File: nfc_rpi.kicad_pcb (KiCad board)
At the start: 2 copper layers, 99.1 x 99.1 mm, 32 parts, among them J1 Raspberry_Pi_zero_2w, J2 OledSpiST1306, J3 OledSpiST7789, SW1 mclr, SW5 mclr

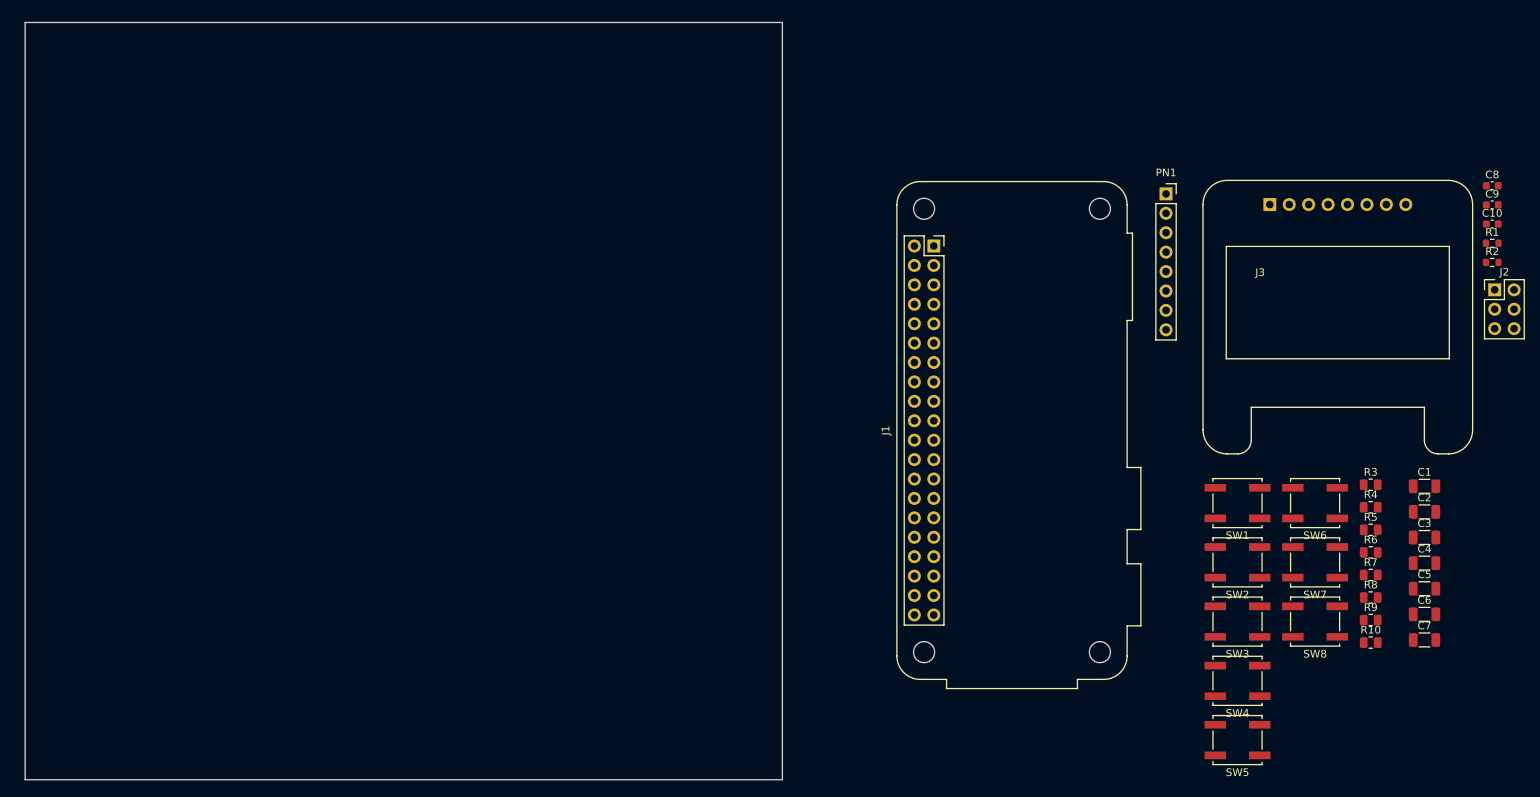
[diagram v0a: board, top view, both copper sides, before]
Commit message: Add hierarchical labels/pins across all sheets, fix DiscoveryAnalog3 rename, PCB 99x99mm rounded corners
- nfc_rpi.kicad_sch: 19 hierarchical pins on PN532 sheet
- pn532.kicad_sch: 22 hierarchical labels with _PN532 suffix
- raspberry_pn532.kicad_sch: 68 hierarchical labels for J1
- nfc.kicad_sch: 54 signal pins on Raspberry sheet, power pins removed
- switch.kicad_sch: 8 switch+resistor circuits with hierarchical labels
- oled.kicad_sch: 7 hierarchical labels
- DiscoveryAnalog3.kicad_sch: 26 hierarchical labels for J4 connector
- nfc_rpi.kicad_pcb: 99x99mm board outline with 5mm rounded corners (gr_line + gr_arc)
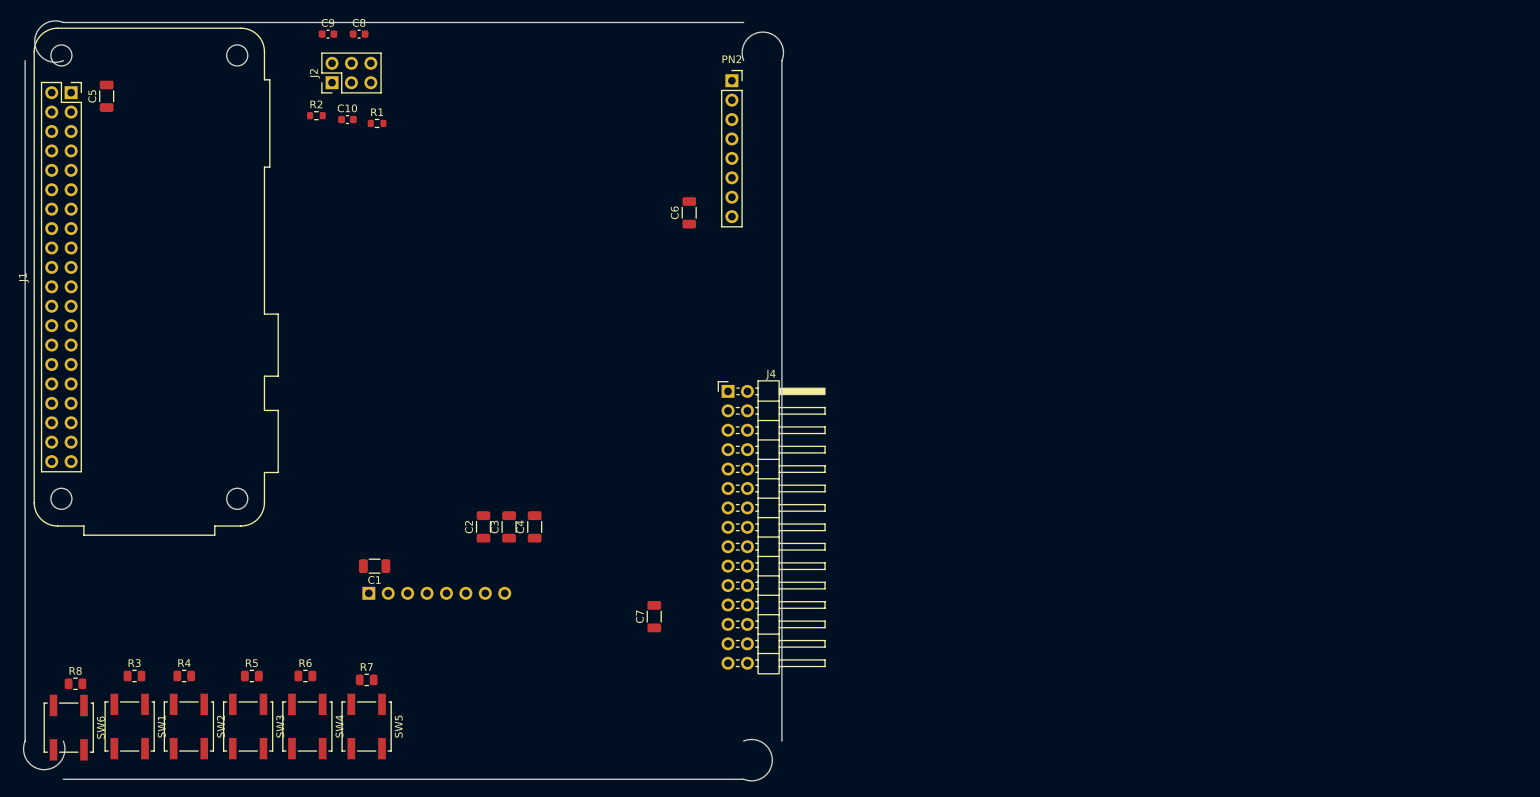
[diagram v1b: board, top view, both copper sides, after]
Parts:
- removed PN1: PN532, Connector_PinSocket_2.54mm:PinSocket_1x08_P2.54mm_Vertical
- removed R10, R9: ~, Resistor_SMD:R_0805_2012Metric
- removed SW7, SW8: ~, Button_Switch_SMD:SW_Push_1P1T_NO_CK_KSC6xxJ
- added J4: Conn_02x15_Odd_Even, Connector_PinHeader_2.54mm:PinHeader_2x15_P2.54mm_Horizontal, F.Cu at (142.7, 99.1)
- added PN2: PN532, Connector_PinSocket_2.54mm:PinSocket_1x08_P2.54mm_Vertical, F.Cu at (143.3, 58.4)
- J3: moved to B.Cu
- SW1, SW5: value mclr -> ~
- moved C5 184.0 mm to (61.5, 60.5), turned to 90 degrees
- moved R8 169.8 mm to (57.4, 137.3)
- moved SW6 165.7 mm to (56.5, 143.0), turned to 90 degrees
- moved R3 163.6 mm to (65.1, 136.3)
- moved R4 156.8 mm to (71.6, 136.3)
- moved R2 155.0 mm to (88.9, 63.0)
- moved J2 154.5 mm to (90.9, 58.7), turned to 90 degrees
- moved C9 153.9 mm to (90.4, 52.3)
- moved C10 150.4 mm to (93.0, 63.5)
- moved C8 149.5 mm to (94.5, 52.3)
- moved SW1 147.8 mm to (64.5, 142.9), turned to 90 degrees
- moved R5 147.6 mm to (80.5, 136.3)
- moved R1 146.7 mm to (96.8, 64.0)
- moved R6 140.3 mm to (87.5, 136.3)
- moved SW2 138.8 mm to (72.2, 142.9), turned to 90 degrees
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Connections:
- net BLK_OLED_RP2040 renamed /oled/BLK_OLED
- net DC_OLED_RP2040 renamed /oled/DC_OLED
- net GPIO24 renamed /swicth/sw4
- net GPIO25 renamed /swicth/sw3
- net GPIO26 renamed /swicth/sw2
- net GPIO27 renamed /swicth/sw1
- net GPIO28 renamed /swicth/sw5
- net RES_OLED_RP2040 renamed /oled/RES_OLED
- net SCL_OLED_RPI renamed /oled/SCL_OLED
- net SDA_OLED_RPI renamed /oled/SDA_OLED
- C1 pad 2: Net-(C1-Pad2) -> GND
- C2 pad 2: Net-(C1-Pad2) -> GND
- C3 pad 2: Net-(C1-Pad2) -> GND
- C4 pad 2: Net-(C1-Pad2) -> GND
- C5 pad 2: Net-(C1-Pad2) -> GND
- C6 pad 2: Net-(C1-Pad2) -> GND
- C7 pad 2: Net-(C1-Pad2) -> GND
- J1 pad 1: unconnected-(J1-3V3-Pad1) -> Net-(J1-3V3-Pad1)
- J1 pad 10: unconnected-(J1-GPIO15/RXD-Pad10) -> /Raspberry/GPIO15/RXD
- J1 pad 11: unconnected-(J1-GPIO17-Pad11) -> /Raspberry/GPIO17
- J1 pad 12: unconnected-(J1-GPIO18/PWM0-Pad12) -> /Raspberry/GPIO18/PWM0
- J1 pad 13: unconnected-(J1-GPIO27-Pad13) -> /Raspberry/GPIO27
- J1 pad 15: unconnected-(J1-GPIO22-Pad15) -> /Raspberry/GPIO22
- J1 pad 16: unconnected-(J1-GPIO23-Pad16) -> /Raspberry/GPIO23
- J1 pad 17: unconnected-(J1-3V3-Pad17) -> Net-(J1-3V3-Pad1)
- J1 pad 18: unconnected-(J1-GPIO24-Pad18) -> /Raspberry/GPIO24
- J1 pad 19: unconnected-(J1-MOSI0/GPIO10-Pad19) -> /Raspberry/MOSI0/GPIO10
- J1 pad 21: Net-(J1-MISO0/GPIO9) -> /Raspberry/MISO0/GPIO9
- J1 pad 22: unconnected-(J1-GPIO25-Pad22) -> /Raspberry/GPIO25
- J1 pad 23: Net-(J1-SCLK0/GPIO11) -> /Raspberry/SCLK0/GPIO11
- J1 pad 24: unconnected-(J1-~{CE0}/GPIO8-Pad24) -> /Raspberry/~{CE0}/GPIO8
- J1 pad 26: unconnected-(J1-~{CE1}/GPIO7-Pad26) -> /Raspberry/~{CE1}/GPIO7
- J1 pad 27: unconnected-(J1-ID_SD/GPIO0-Pad27) -> /Raspberry/ID_SD/GPIO0
- J1 pad 28: unconnected-(J1-ID_SC/GPIO1-Pad28) -> /Raspberry/ID_SC/GPIO1
- J1 pad 29: Net-(J1-GCLK1/GPIO5) -> /Raspberry/GCLK1/GPIO5
- J1 pad 3: Net-(J1-SDA/GPIO2) -> /Raspberry/SDA/GPIO2
- J1 pad 31: Net-(J1-GCLK2/GPIO6) -> /Raspberry/GCLK2/GPIO6
- J1 pad 32: unconnected-(J1-PWM0/GPIO12-Pad32) -> /Raspberry/PWM0/GPIO12
- J1 pad 33: unconnected-(J1-PWM1/GPIO13-Pad33) -> /Raspberry/PWM1/GPIO13
- J1 pad 35: unconnected-(J1-GPIO19/MISO1-Pad35) -> /Raspberry/GPIO19/MISO1
- J1 pad 36: unconnected-(J1-GPIO16-Pad36) -> /Raspberry/GPIO16
- J1 pad 37: unconnected-(J1-GPIO26-Pad37) -> /Raspberry/GPIO26
- J1 pad 38: unconnected-(J1-GPIO20/MOSI1-Pad38) -> /Raspberry/GPIO20/MOSI1
- J1 pad 4: unconnected-(J1-GPIO4-Pad4) -> /Raspberry/GPIO4
- J1 pad 40: unconnected-(J1-GPIO21/SCLK1-Pad40) -> /Raspberry/GPIO21/SCLK1
- J1 pad 5: Net-(J1-SCL/GPIO3) -> /Raspberry/SCL/GPIO3
- J1 pad 7: unconnected-(J1-GCLK0/GPIO4-Pad7) -> /Raspberry/GCLK0/GPIO4
- J1 pad 8: unconnected-(J1-GPIO14/TXD-Pad8) -> /Raspberry/GPIO14/TXD
- J3 pad 2: +5V -> +3V3
- R8 pad 1: GPIO29 -> /swicth/sw6
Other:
- board size 99.1 x 99.1 mm -> 99.4 x 99.4 mm
